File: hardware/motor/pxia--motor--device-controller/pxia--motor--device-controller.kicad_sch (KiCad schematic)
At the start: 16 parts

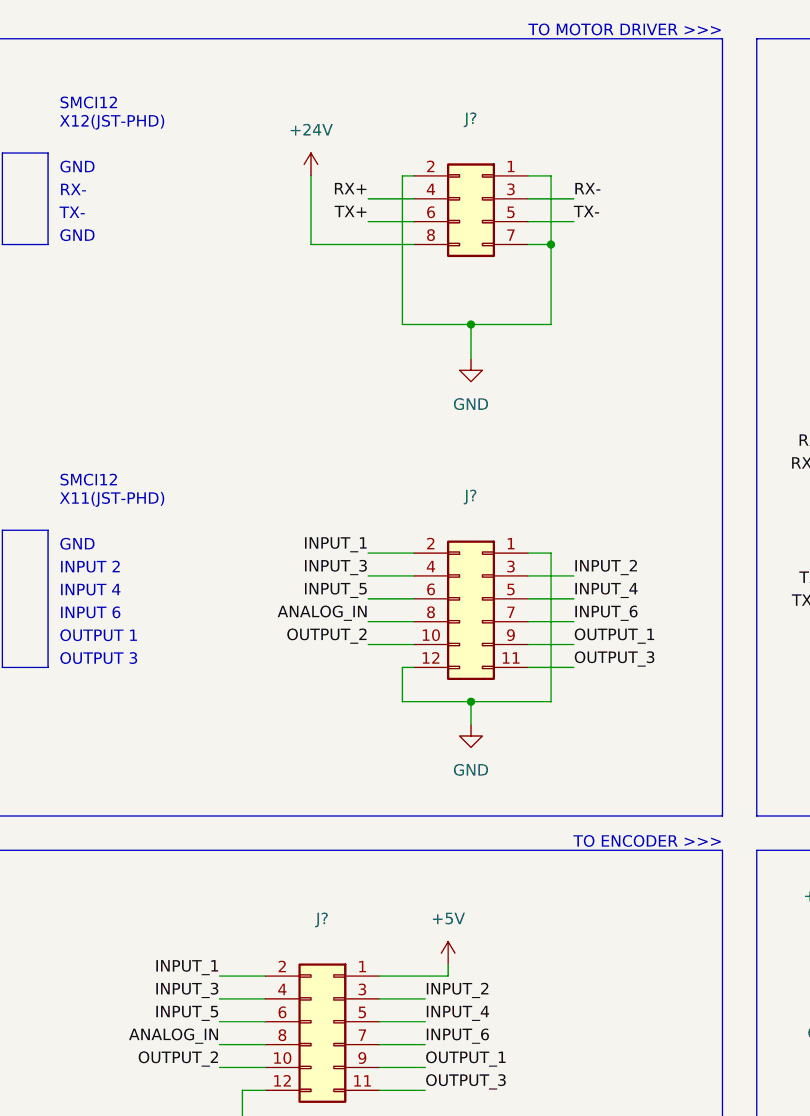
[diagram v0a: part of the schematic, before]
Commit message: updated schematics + footprint
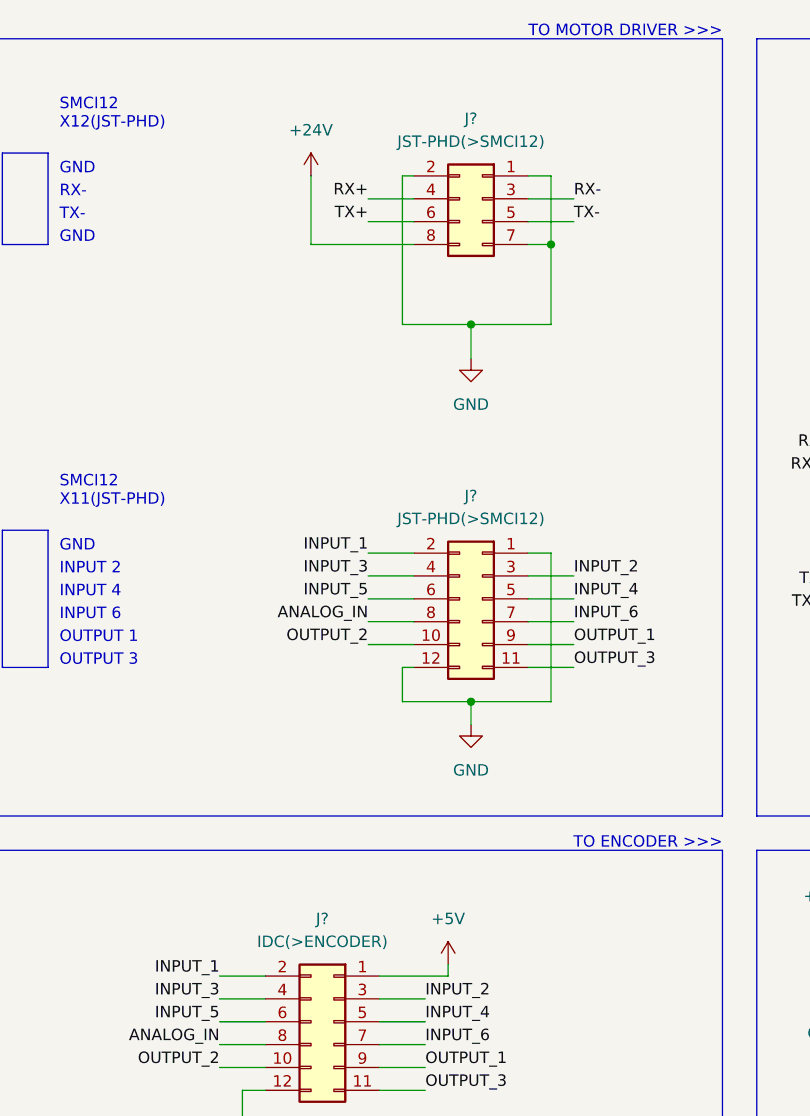
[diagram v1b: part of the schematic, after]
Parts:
- J? (x2): value (none) -> JST-PHD(>SMCI12)
- J?: value (none) -> IDC(>ENCODER)
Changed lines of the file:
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@@
     (in_bom yes) (on_board yes) (fields_autoplaced)
     (property "Reference" "J?" (id 0) (at 87.63 72.39 0))
-    (property "Value" "" (id 1) (at 87.63 74.93 0))
+    (property "Value" "JST-PHD(>SMCI12)" (id 1) (at 87.63 74.93 0))
     (property "Footprint" "" (id 2) (at 88.9 83.82 0)
       (effects (font (size 1.27 1.27)) hide)
@@
     (in_bom yes) (on_board yes) (fields_autoplaced)
     (property "Reference" "J?" (id 0) (at 87.63 30.48 0))
-    (property "Value" "" (id 1) (at 87.63 33.02 0))
+    (property "Value" "JST-PHD(>SMCI12)" (id 1) (at 87.63 33.02 0))
     (property "Footprint" "" (id 2) (at 88.9 39.37 0)
       (effects (font (size 1.27 1.27)) hide)
@@
     (in_bom yes) (on_board yes)
     (property "Reference" "J?" (id 0) (at 71.12 119.38 0))
-    (property "Value" "" (id 1) (at 71.12 121.92 0))
+    (property "Value" "IDC(>ENCODER)" (id 1) (at 71.12 121.92 0))
     (property "Footprint" "" (id 2) (at 72.39 130.81 0)
       (effects (font (size 1.27 1.27)) hide)

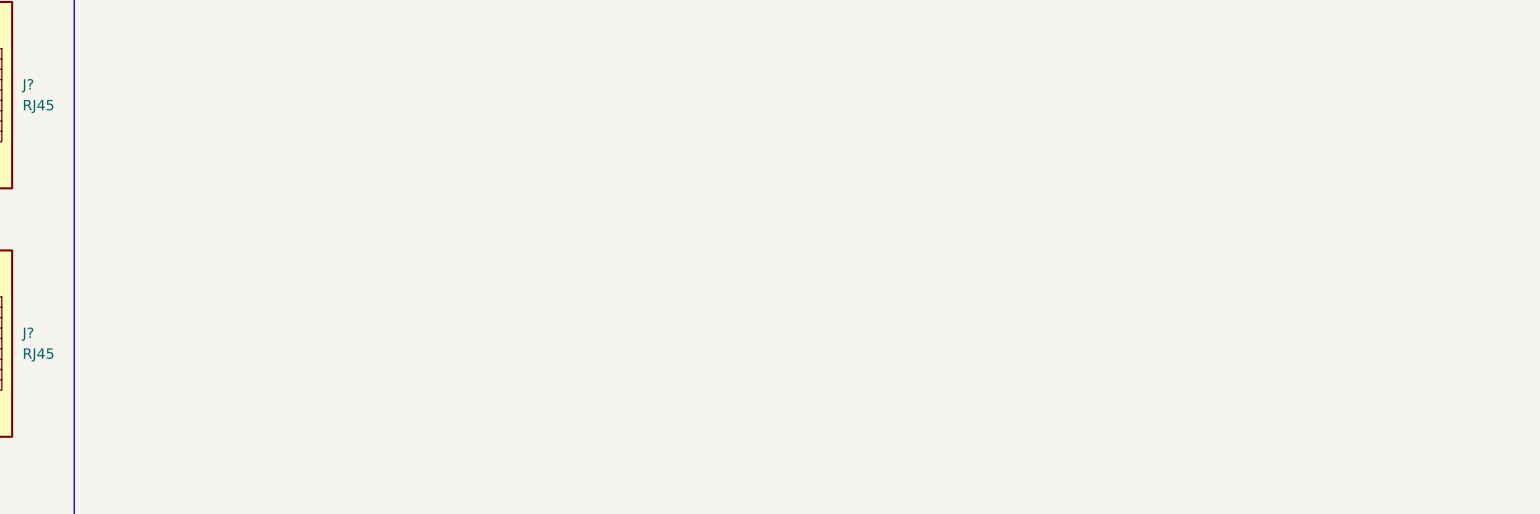
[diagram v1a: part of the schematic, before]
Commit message: added drawing, added ESP32 to host board
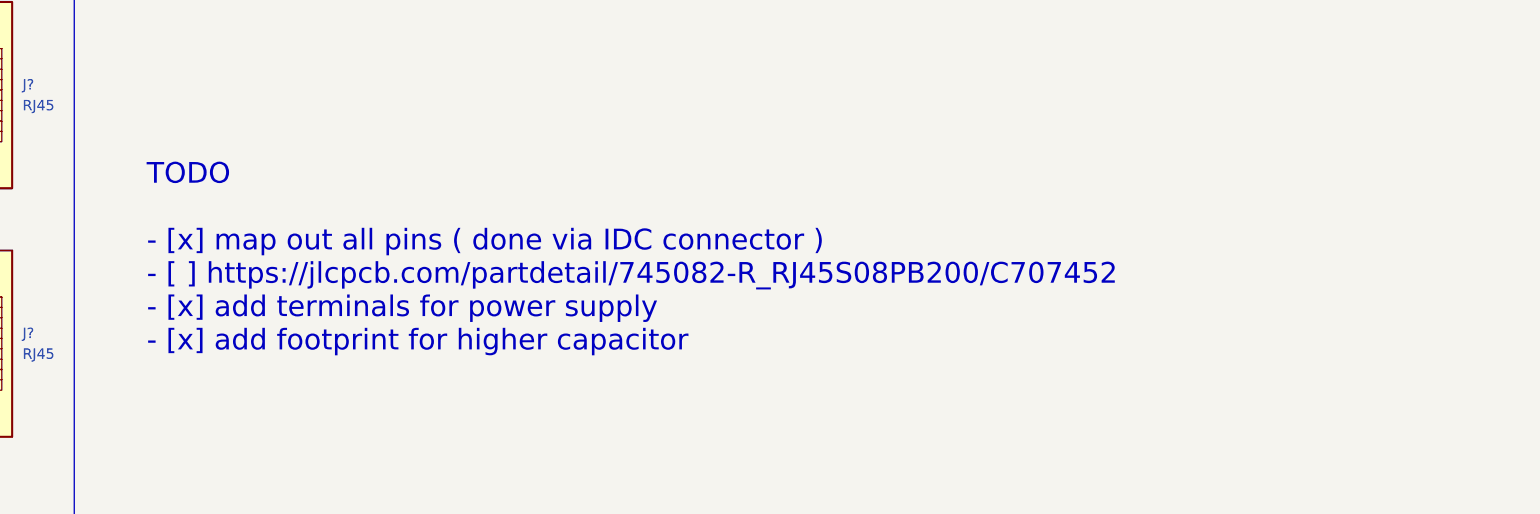
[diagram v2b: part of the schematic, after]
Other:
- note added: "TODO - [x] map out all pins ( done via IDC connector ) -﻿ [ ] https://jlcpcb.com/partdetail/745082-R_RJ45S08PB200/C707452 - [x] add terminals for power supply - [x] add footprint for higher capacitor"
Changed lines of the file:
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@@
     (effects (font (size 1.27 1.27)) (justify right bottom))
+  )
+  (text "TODO\n\n- [x] map out all pins ( done via IDC connector )\n-﻿ [ ] https://jlcpcb.com/partdetail/745082-R_RJ45S08PB200/C707452\n- [x] add terminals for power supply \n- [x] add footprint for higher capacitor"
+    (at 228.6 77.47 0)
+    (effects (font (size 2.54 2.54)) (justify left bottom))
   )
   (text "SMCI12\nX11(JST-PHD)" (at 41.91 73.66 0)

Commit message: finished schematics and most of pcb layout
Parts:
- removed H? (x2): M3, symbol Mechanical:MountingHole
- removed J?: JST-PHD(>SMCI12), symbol Connector_Generic:Conn_02x06_Odd_Even
- removed J?: JST-PHD(>SMCI12), symbol Connector_Generic:Conn_02x04_Odd_Even
- removed J?: IDC(>ENCODER), symbol Connector_Generic:Conn_02x06_Odd_Even
- added J1: IDC(>ENC), Connector_Molex:Molex_Nano-Fit_105314-xx12_2x06_P2.50mm_Horizontal, symbol Connector_Generic:Conn_02x06_Top_Bottom
- added J2: JST-PHD(>SMCI12(X12)), Connector_JST:JST_PHD_S8B-PHDSS_2x04_P2.00mm_Horizontal, symbol Connector_Generic:Conn_02x04_Odd_Even
- added J3: JST-PHD(>SMCI12(X11)), Connector_JST:JST_PHD_S12B-PHDSS_2x06_P2.00mm_Horizontal, symbol Connector_Generic:Conn_02x06_Odd_Even
- C1: renamed from C?; footprint (none) -> Capacitor_THT:CP_Radial_D18.0mm_P7.50mm
- C2, C3: renamed from C?; footprint (none) -> Capacitor_SMD:C_1206_3216Metric_Pad1.33x1.80mm_HandSolder
- H2, H4: renamed from H?; footprint (none) -> MountingHole:MountingHole_3.2mm_M3
- J4: renamed from J?; footprint (none) -> TerminalBlock:TerminalBlock_bornier-2_P5.08mm
- J5, J6: renamed from J?; footprint (none) -> Connector_RJ:RJ45_OST_PJ012-8P8CX_Vertical
- R1, R2: renamed from R?; footprint (none) -> Resistor_SMD:R_0805_2012Metric_Pad1.20x1.40mm_HandSolder
- gave numbers to parts that had none: 1
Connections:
- net +24V: now also J4.2 (Pin_2), J2.2 (Pin_2); no longer J4.1 (Pin_1)
- net +5V: now also J1.1 (Pin_1)
- net ANALOG_IN: now also J1.8 (Pin_8), J3.6 (Pin_6)
- net GND: now also J4.1 (Pin_1), J1.12 (Pin_12), J2.1 (Pin_1), J2.7 (Pin_7), J2.8 (Pin_8), J3.11 (Pin_11), J3.2 (Pin_2); no longer J4.2 (Pin_2)
- net INPUT_1: now also J1.2 (Pin_2), J3.12 (Pin_12)
- net INPUT_2: now also J1.3 (Pin_3), J3.9 (Pin_9)
- net INPUT_3: now also J1.4 (Pin_4), J3.10 (Pin_10)
- net INPUT_4: now also J1.5 (Pin_5), J3.7 (Pin_7)
- net INPUT_5: now also J1.6 (Pin_6), J3.8 (Pin_8)
- net INPUT_6: now also J1.7 (Pin_7), J3.5 (Pin_5)
- net OUTPUT_1: now also J1.9 (Pin_9), J3.3 (Pin_3)
- net OUTPUT_2: now also J1.10 (Pin_10), J3.4 (Pin_4)
- net OUTPUT_3: now also J1.11 (Pin_11), J3.1 (Pin_1)
- net RX+: now also J2.6 (Pin_6)
- net RX-: now also J2.5 (Pin_5)
- net TX+: now also J2.4 (Pin_4)
- net TX-: now also J2.3 (Pin_3)
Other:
- note added: "1"
- note added: "10"
- note added: "11"
- note added: "12"
- note added: "2"
- note added: "3"
- note added: "4"
- note added: "5"
- note added: "6"
- note added: "7"
- note added: "8"
- note added: "9"
- note added: "@TODO(are *terminal resistors* also required on motor driver side? maybe DNF?)"
- note added: "MFR.Part # 5555799-1"
- note added: "MFR.Part # LM7805CT"
- note added: "mounting holes aligned with SMCI12 PCB mounting holes"
- note added: "Ø18.3mm"
- note removed: "@TODO(are *terminal resistor* also required on motor driver side? maybe DNF?)"
- note removed: "mounting holes aligned to SMCI12 PCB mounting holes."
- note removed: "Ø25mm?"

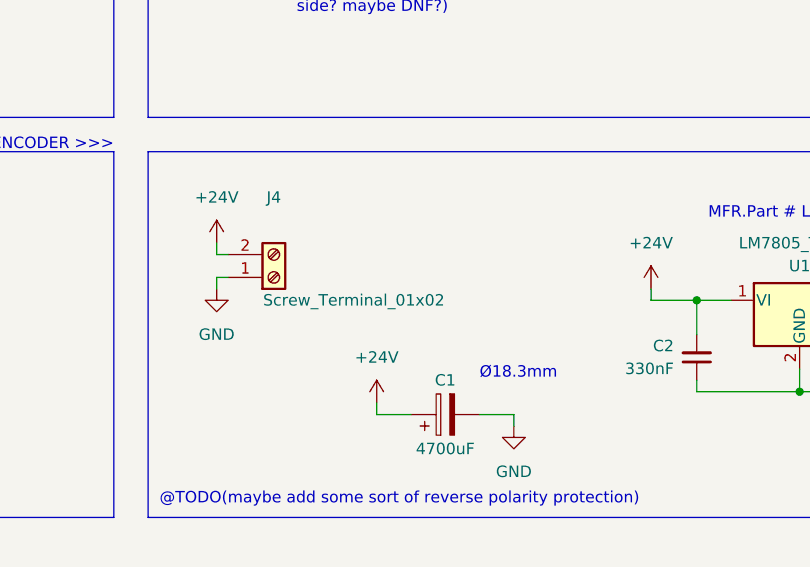
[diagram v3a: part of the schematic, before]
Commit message: added PicoW, finished PCB layout
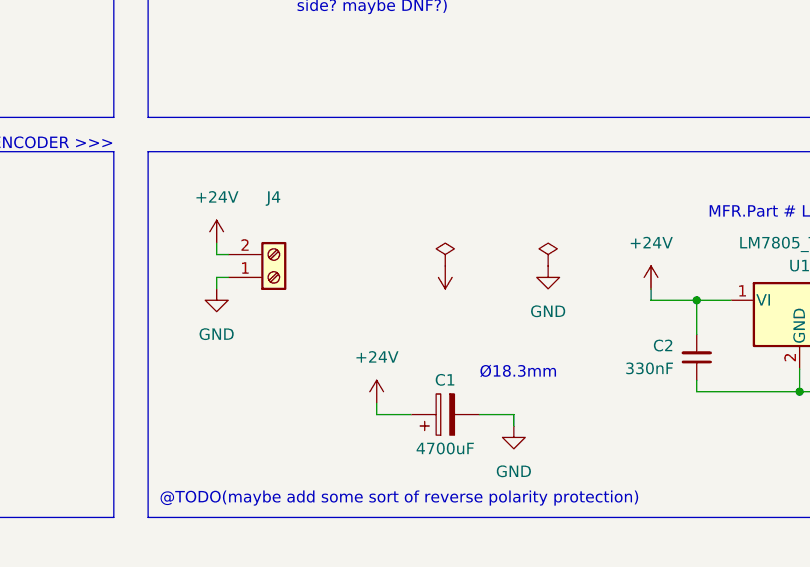
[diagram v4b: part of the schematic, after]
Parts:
- J4: value Screw_Terminal_01x02 -> (none)
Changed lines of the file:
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@@
     (pin "8")
+  )
+  (symbol (lib_id "power:+24V") (at 152.4 124.46 180) (unit 1)
+    (in_bom yes) (on_board yes)
+    (property "Reference" "#PWR01" (id 0) (at 152.4 120.65 0)
+      (effects (font (size 1.27 1.27)) hide)
+    )
+    (property "Value" "" (id 1) (at 152.4 129.54 0))
+    (property "Footprint" "" (id 2) (at 152.4 124.46 0)
+      (effects (font (size 1.27 1.27)) hide)
+    )
+    (property "Datasheet" "" (id 3) (at 152.4 124.46 0)
+      (effects (font (size 1.27 1.27)) hide)
+    )
+    (pin "1")
   )
   (symbol (lib_id "power:GND") (at 102.87 46.99 0) (unit 1)
@@
     (pin "1")
   )
+  (symbol (lib_id "power:GND") (at 163.83 124.46 0) (unit 1)
+    (in_bom yes) (on_board yes) (fields_autoplaced)
+    (property "Reference" "#PWR03" (id 0) (at 163.83 130.81 0)
+      (effects (font (size 1.27 1.27)) hide)
+    )
+    (property "Value" "GND" (id 1) (at 163.83 129.54 0))
+    (property "Footprint" "" (id 2) (at 163.83 124.46 0)
+      (effects (font (size 1.27 1.27)) hide)
+    )
+    (property "Datasheet" "" (id 3) (at 163.83 124.46 0)
+      (effects (font (size 1.27 1.27)) hide)
+    )
+    (pin "1")
+  )
+  (symbol (lib_id "power:PWR_FLAG") (at 152.4 124.46 0) (unit 1)
+    (in_bom yes) (on_board yes) (fields_autoplaced)
+    (property "Reference" "#FLG01" (id 0) (at 152.4 122.555 0)
+      (effects (font (size 1.27 1.27)) hide)
+    )
+    (property "Value" "" (id 1) (at 152.4 119.38 0))
+    (property "Footprint" "" (id 2) (at 152.4 124.46 0)
+      (effects (font (size 1.27 1.27)) hide)
+    )
+    (property "Datasheet" "~" (id 3) (at 152.4 124.46 0)
+      (effects (font (size 1.27 1.27)) hide)
+    )
+    (pin "1")
+  )
   (symbol (lib_id "power:GND") (at 101.6 90.17 0) (unit 1)
     (in_bom yes) (on_board yes)
@@
     (pin "9")
   )
+  (symbol (lib_id "power:PWR_FLAG") (at 163.83 124.46 0) (unit 1)
+    (in_bom yes) (on_board yes) (fields_autoplaced)
+    (property "Reference" "#FLG03" (id 0) (at 163.83 122.555 0)
+      (effects (font (size 1.27 1.27)) hide)
+    )
+    (property "Value" "" (id 1) (at 163.83 119.38 0))
+    (property "Footprint" "" (id 2) (at 163.83 124.46 0)
+      (effects (font (size 1.27 1.27)) hide)
+    )
+    (property "Datasheet" "~" (id 3) (at 163.83 124.46 0)
+      (effects (font (size 1.27 1.27)) hide)
+    )
+    (pin "1")
+  )
   (symbol (lib_id "Device:C_Polarized") (at 152.4 140.97 90) (unit 1)
     (in_bom yes) (on_board yes)
@@
     (in_bom yes) (on_board yes)
     (property "Reference" "J4" (id 0) (at 133.35 116.84 0))
-    (property "Value" "Screw_Terminal_01x02" (id 1) (at 142.24 128.27 0))
+    (property "Value" "" (id 1) (at 138.43 129.54 0))
     (property "Footprint" "TerminalBlock:TerminalBlock_bornier-2_P5.08mm" (id 2) (at 133.35 125.73 0)
       (effects (font (size 1.27 1.27)) hide)
@@
   )
   (symbol_instances
+    (path "/94b23249-443d-4371-8390-5abe68368d28"
+      (reference "#FLG01") (unit 1) (value "PWR_FLAG") (footprint "")
+    )
+    (path "/c4c1e2d2-6d8c-4f89-af1b-cb13ef290181"
+      (reference "#FLG03") (unit 1) (value "PWR_FLAG") (footprint "")
+    )
+    (path "/30a840a7-6ecb-443a-86b6-8462e8f4909a"
+      (reference "#PWR01") (unit 1) (value "+24V") (footprint "")
+    )
+    (path "/898647c7-9037-4ec0-9012-9d1cffa89f38"
+      (reference "#PWR03") (unit 1) (value "GND") (footprint "")
+    )
     (path "/25e750f9-bb53-4a5d-b5b8-0532f17962fd"
       (reference "#PWR0101") (unit 1) (value "+24V") (footprint "")
@@
     )
     (path "/f5703396-3ce6-4354-b139-6f7277aeeb02"
-      (reference "J4") (unit 1) (value "Screw_Terminal_01x02") (footprint "TerminalBlock:TerminalBlock_bornier-2_P5.08mm")
+      (reference "J4") (unit 1) (value "PWR_SUPPLY") (footprint "TerminalBlock:TerminalBlock_bornier-2_P5.08mm")
     )
     (path "/2f5c81a1-38bc-453f-b609-2e1ffc594655"

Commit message: cleaned up, production ready
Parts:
- C1: value 4700uF -> (none); footprint Capacitor_THT:CP_Radial_D18.0mm_P7.50mm -> (none); LCSC (none) -> DNF
- C2: value 330nF -> (none); footprint Capacitor_SMD:C_1206_3216Metric_Pad1.33x1.80mm_HandSolder -> (none); LCSC (none) -> C307572
- C3: value 100nF -> (none); footprint Capacitor_SMD:C_1206_3216Metric_Pad1.33x1.80mm_HandSolder -> (none); LCSC (none) -> C1945
- H2, H4: value M3 -> (none); footprint MountingHole:MountingHole_3.2mm_M3 -> (none); LCSC (none) -> DNF
- J1: value IDC(>ENC) -> (none); footprint Connector_Molex:Molex_Nano-Fit_105314-xx12_2x06_P2.50mm_Horizontal -> (none); LCSC (none) -> DNF
- J2: value JST-PHD(>SMCI12(X12)) -> (none); footprint Connector_JST:JST_PHD_S8B-PHDSS_2x04_P2.00mm_Horizontal -> (none); LCSC (none) -> DNF
- J3: value JST-PHD(>SMCI12(X11)) -> (none); footprint Connector_JST:JST_PHD_S12B-PHDSS_2x06_P2.00mm_Horizontal -> (none); LCSC (none) -> DNF
- J4: footprint TerminalBlock:TerminalBlock_bornier-2_P5.08mm -> (none); LCSC (none) -> C474881
- J5, J6: value RJ45 -> (none); footprint Connector_RJ:RJ45_OST_PJ012-8P8CX_Vertical -> (none); LCSC (none) -> C305983
- R1, R2: value 120R -> (none); footprint Resistor_SMD:R_0805_2012Metric_Pad1.20x1.40mm_HandSolder -> (none); LCSC (none) -> C114244
- U1: value LM7805_TO220 -> (none); footprint Package_TO_SOT_THT:TO-220-3_Vertical -> (none); LCSC (none) -> C50931
